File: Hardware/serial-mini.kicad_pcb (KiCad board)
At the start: 4 copper layers, 97 x 42 mm, 79 parts, among them J1 PICKIT V3 Header, J2 10103593-0001LF, J3 Serial Port, Q1 IRLML2060, Q2 IRLML2060, Q3 IRLML2060, U1 MAX232, U2 SN74AHC14RGYR, U3 DSPIC33CK64MP102, U4 MIC5504-3.3YM5-TR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

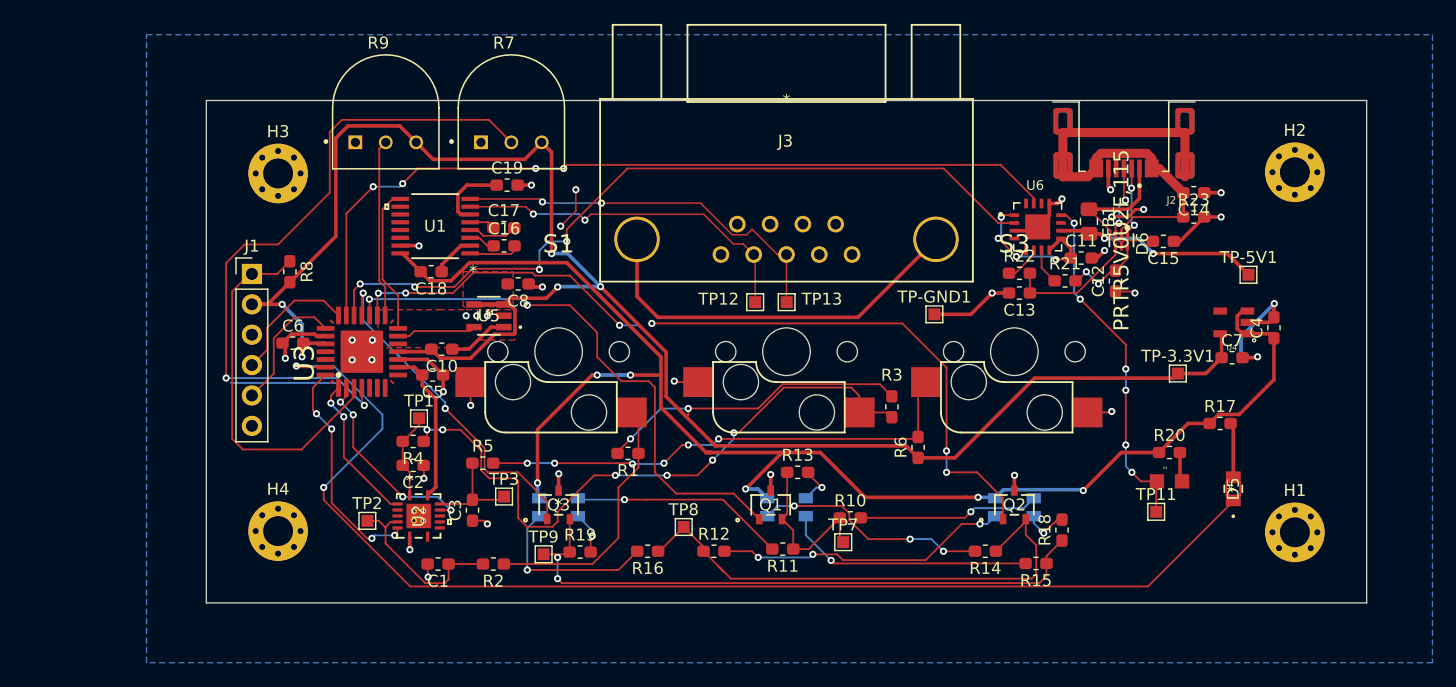
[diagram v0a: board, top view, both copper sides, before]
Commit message: Fix incorrect footprints
Fixed incorrect footprint for IRLML2060 and updated LED values to use CLVBA-FKA.
Also started deleting unneccessary test points
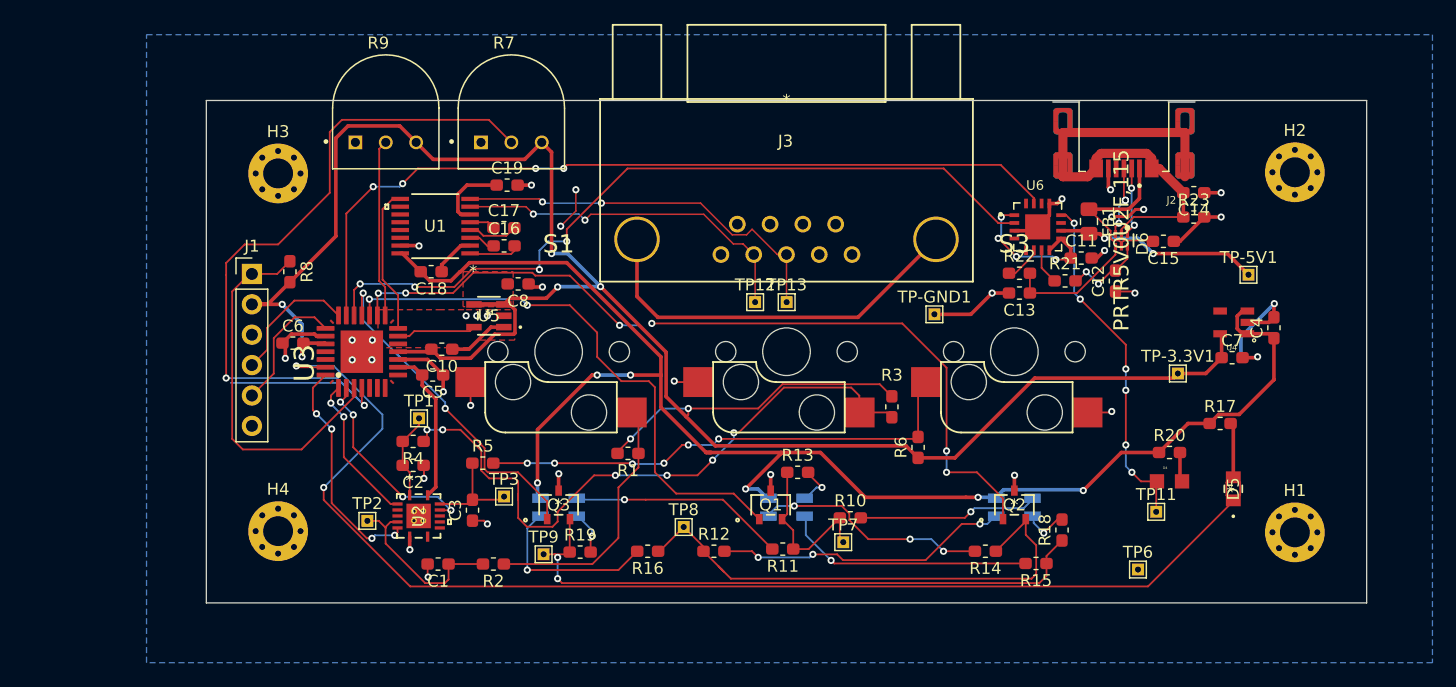
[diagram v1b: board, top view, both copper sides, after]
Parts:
- added TP6: TestPoint, TestPoint:TestPoint_THTPad_1.0x1.0mm_Drill0.5mm, F.Cu at (164.1, 108.5)
- D1, D2, D3: footprint footprints:CLVBA-FKA-CAEDH8BBB7A363 -> footprints:SOL150P350X210-4N
- R10, R11, R13: value 74 -> 100
- R12, R14, R16: value 130 -> 155
- R15, R18, R19: value 90 -> 100
- TP-3.3V1, TP-5V1, TP-GND1, TP1, TP11, TP12, TP13, TP2, TP3, TP7, TP8, TP9: footprint TestPoint:TestPoint_Pad_1.0x1.0mm -> TestPoint:TestPoint_THTPad_1.0x1.0mm_Drill0.5mm
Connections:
- Q1 pad 2: /Backlight/1.7V@69mA -> GND
- Q1 pad 3: GND -> /Backlight/2V@60mA
- Q2 pad 2: /Backlight/3V@69mA -> GND
- Q2 pad 3: GND -> /Backlight/3.1V@60mA
- Q3 pad 2: /Backlight/1.7V@57mA -> GND
- Q3 pad 3: GND -> /Backlight/2V@60mA
- R10 pad 1: /Backlight/1.7V@69mA -> /Backlight/2V@60mA
- R11 pad 1: /Backlight/1.7V@69mA -> /Backlight/2V@60mA
- R12 pad 1: /Backlight/3V@69mA -> /Backlight/3.1V@60mA
- R13 pad 1: /Backlight/1.7V@69mA -> /Backlight/2V@60mA
- R14 pad 1: /Backlight/3V@69mA -> /Backlight/3.1V@60mA
- R15 pad 1: /Backlight/1.7V@57mA -> /Backlight/2V@60mA
- R16 pad 1: /Backlight/3V@69mA -> /Backlight/3.1V@60mA
- R18 pad 1: /Backlight/1.7V@57mA -> /Backlight/2V@60mA
- R19 pad 1: /Backlight/1.7V@57mA -> /Backlight/2V@60mA
- TP7 pad 1: /Backlight/1.7V@69mA -> /Backlight/2V@60mA
- TP8 pad 1: /Backlight/3V@69mA -> /Backlight/3.1V@60mA
- TP9 pad 1: /Backlight/1.7V@57mA -> /Backlight/2V@60mA
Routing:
- net GND: track 75.9 -> 71.8 mm, vias 35 -> 32
- net /Backlight/2V@60mA: track 0.00 -> 2.76 mm, vias 0 -> 2
- net /Backlight/3.1V@60mA: track 0.00 -> 1.29 mm, vias 0 -> 1

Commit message: Fix DRC errors
Courtyard overlaps
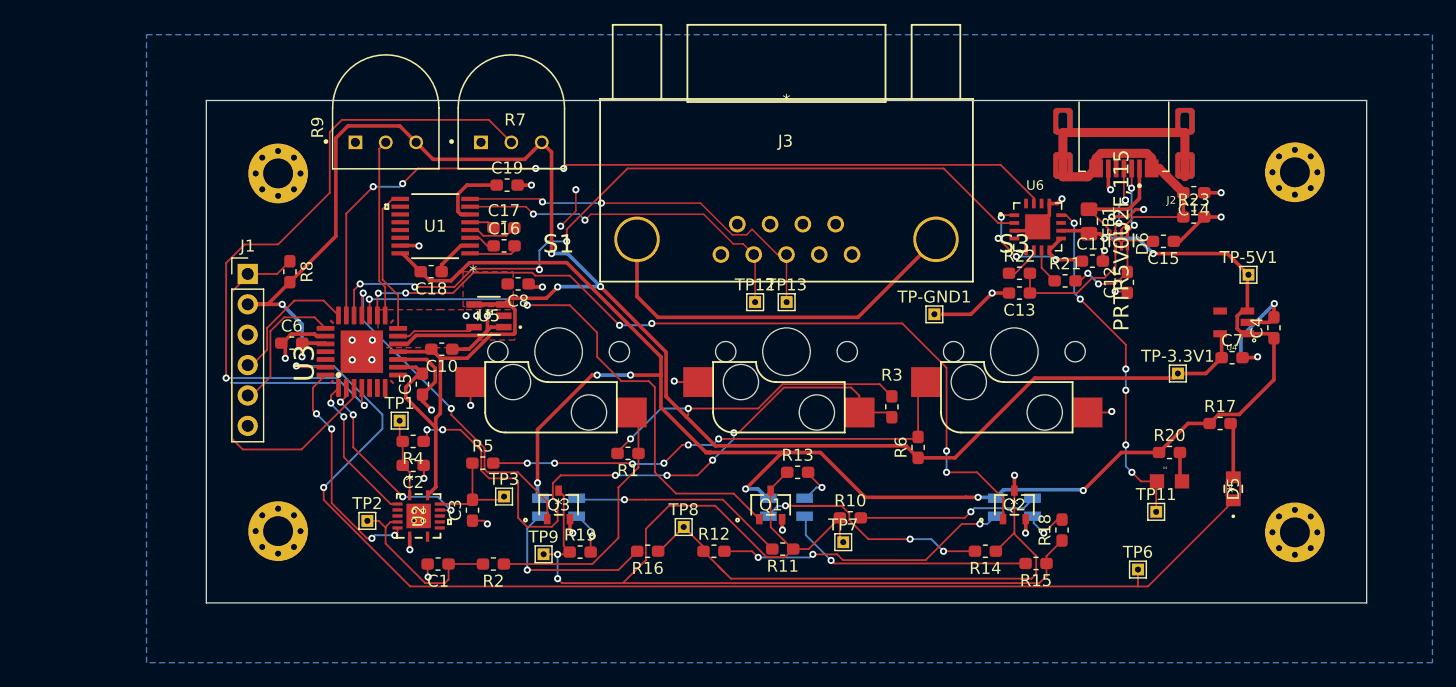
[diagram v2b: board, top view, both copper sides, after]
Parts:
- moved TP1 1.63 mm to (102.4, 96.0)
- moved C5 1.15 mm to (104.3, 93.0), turned to 90 degrees
- moved C12 1.00 mm to (163.2, 84.5)
- moved C11 0.97 mm to (160.3, 82.7)
- moved J1 0.35 mm to (89.7, 83.7)
- moved C6 0.10 mm to (93.3, 89.5)
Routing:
- net /Backlight/2V@60mA: track 2.76 -> 90.1 mm
- net /Backlight/1.7V@57mA: track 51.9 -> 0.00 mm, vias 2 -> 0
- net /Backlight/3.1V@60mA: track 1.29 -> 46.7 mm
- net /Backlight/3V@69mA: track 44.2 -> 0.00 mm
- net /Backlight/1.7V@69mA: track 14.1 -> 0.00 mm
- net GND: track 71.8 -> 85.4 mm, vias 32 -> 35
- net +3V3: track 194.4 -> 201.9 mm
- net Net-(D2-Pad1): track 19.6 -> 23.6 mm
- net +5V: track 140.4 -> 143.4 mm
- net Net-(C12-Pad2): track 7.99 -> 10.1 mm
- net Net-(R3-Pad2): track 54.3 -> 56.3 mm
- net Net-(C13-Pad1): track 11.0 -> 12.5 mm
- net /Status: track 102.5 -> 103.9 mm
- net /Red: track 68.4 -> 69.6 mm
- net Net-(C2-Pad2): track 7.59 -> 6.93 mm
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
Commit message: Adjust all track/text widths
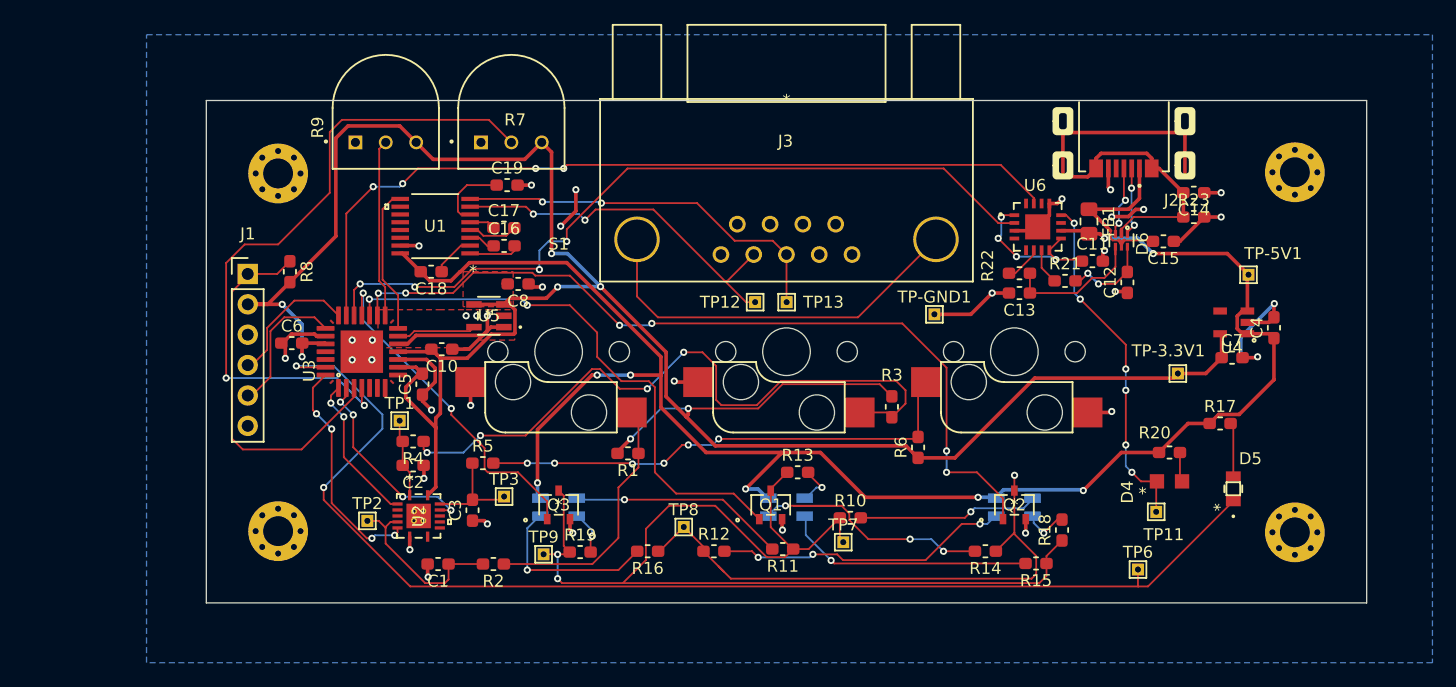
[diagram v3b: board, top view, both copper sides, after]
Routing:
- net /Brightness: track 68.2 -> 58.9 mm
- net /TTL to RS232 Converter/RS232-RX: track 29.8 -> 31.4 mm
- net Net-(R3-Pad2): track 56.3 -> 56.9 mm, vias 6 -> 4
- net /USB to UART/D+: vias 3 -> 2
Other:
- net class Default: clearance 0.127 -> 0.0762; trace_width 0.127 -> 0.1524
- net class Power added: clearance 0.0762, trace_width 0.3048, via_dia 0.6, via_drill 0.3
- rule trace_clearance: 0.127 -> 0.0762
- rule trace_min: 0.127 -> 0.1524

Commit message: Finish placing footprint labels
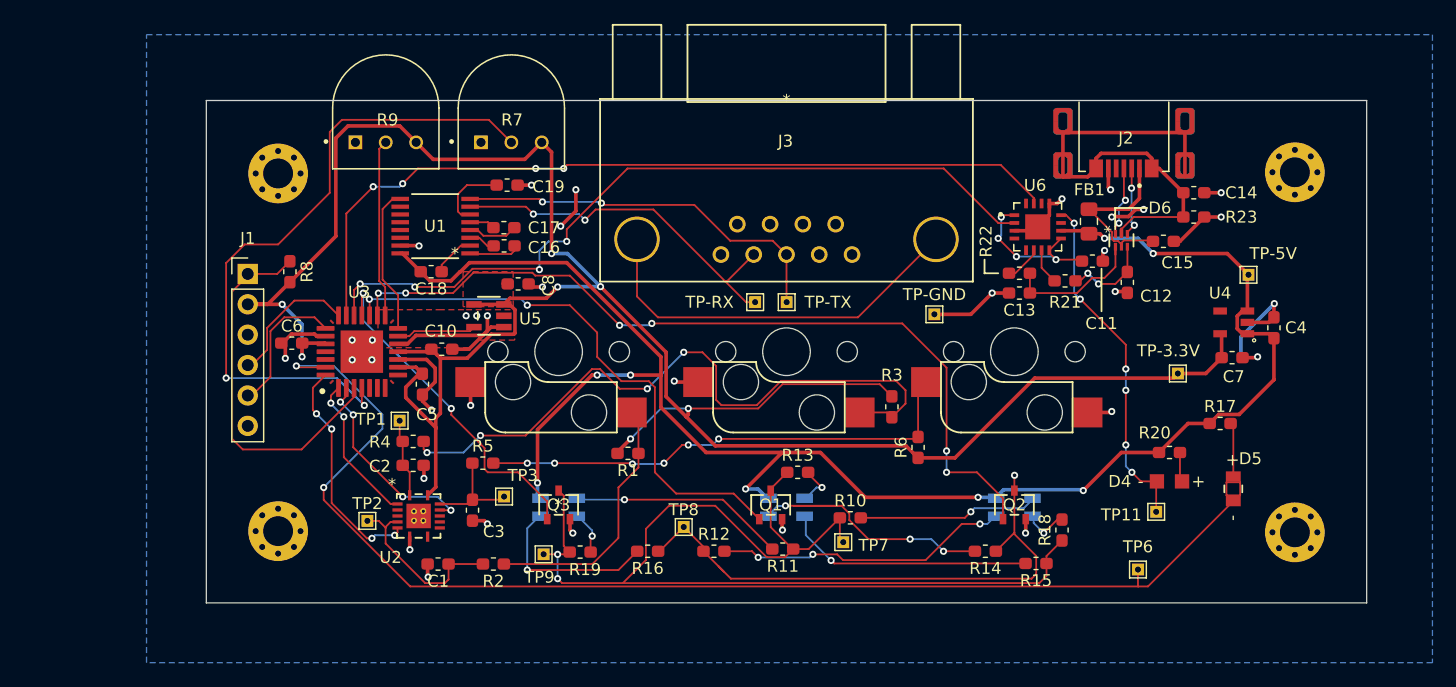
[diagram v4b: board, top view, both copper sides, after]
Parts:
- D5: value VAOL-S8WR4 -> LED_VCCLITE_0805_VCC
- U2: value SN74AHC14RGYR -> RGY14_2P05X2P05
- U5: value SIT2001BI-S2-33S-100.000000D -> SOT_SiT1630-S
- renumbered TP-3.3V1 to TP-3.3V, TP-5V1 to TP-5V, TP-GND1 to TP-GND, TP12 to TP-RX, TP13 to TP-TX

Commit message: Fix faulty debounce circuit
Used wrong value resistor/misplaced on each switch.
Also adjusted value of RC circuits for a time constant of 1 microsecond (was 1 millisecond before)
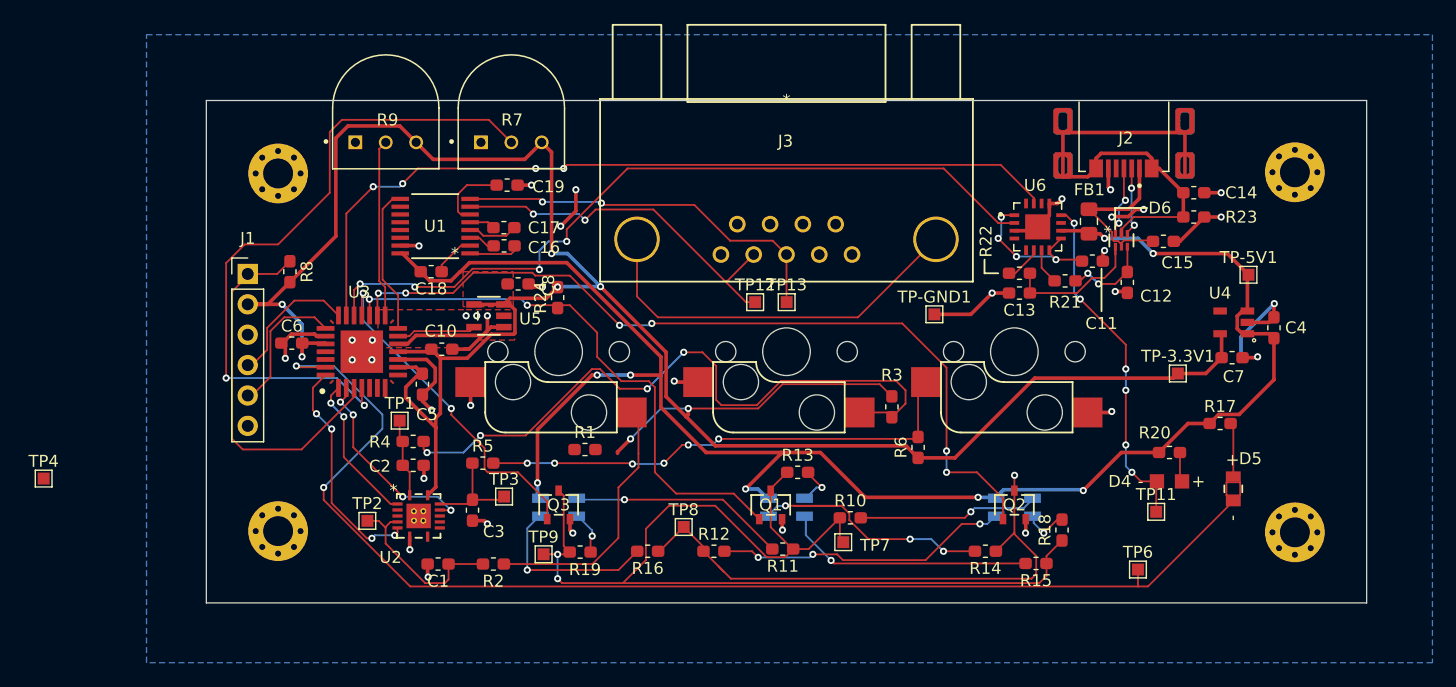
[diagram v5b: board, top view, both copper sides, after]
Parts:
- added R24: 10k, Resistor_SMD:R_0603_1608Metric_Pad1.05x0.95mm_HandSolder, F.Cu at (115.6, 85.7)
- added TP4: TestPoint, TestPoint:TestPoint_Pad_1.0x1.0mm, F.Cu at (72.6, 100.9)
- C1, C2, C3: value 0.1UF -> 10nF
- D5: value LED_VCCLITE_0805_VCC -> VAOL-S8WR4
- R17: value 133 -> 100
- R2, R4, R5: value 10k -> 1k
- TP-3.3V1: renamed from TP-3.3V; footprint TestPoint:TestPoint_THTPad_1.0x1.0mm_Drill0.5mm -> TestPoint:TestPoint_Pad_1.0x1.0mm
- TP-5V1: renamed from TP-5V; footprint TestPoint:TestPoint_THTPad_1.0x1.0mm_Drill0.5mm -> TestPoint:TestPoint_Pad_1.0x1.0mm
- TP-GND1: renamed from TP-GND; footprint TestPoint:TestPoint_THTPad_1.0x1.0mm_Drill0.5mm -> TestPoint:TestPoint_Pad_1.0x1.0mm
- TP1, TP11, TP2, TP3, TP6, TP7, TP8, TP9: footprint TestPoint:TestPoint_THTPad_1.0x1.0mm_Drill0.5mm -> TestPoint:TestPoint_Pad_1.0x1.0mm
- TP12: renamed from TP-RX; footprint TestPoint:TestPoint_THTPad_1.0x1.0mm_Drill0.5mm -> TestPoint:TestPoint_Pad_1.0x1.0mm
- TP13: renamed from TP-TX; footprint TestPoint:TestPoint_THTPad_1.0x1.0mm_Drill0.5mm -> TestPoint:TestPoint_Pad_1.0x1.0mm
- U2: value RGY14_2P05X2P05 -> SN74AHC14RGYR
- U5: value SOT_SiT1630-S -> SIT2001BI-S2-33S-100.000000D
- moved R1 3.61 mm to (117.9, 98.4), turned to 0 degrees
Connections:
- R1 pad 1: Net-(R1-Pad1) -> Net-(C1-Pad1)
- R2 pad 1: Net-(R1-Pad1) -> Net-(R2-Pad1)
- R3 pad 2: Net-(R3-Pad2) -> Net-(C2-Pad2)
- R4 pad 1: Net-(R3-Pad2) -> Net-(R4-Pad1)
- R6 pad 2: Net-(R5-Pad2) -> Net-(C3-Pad2)
- S1 pad 2: Net-(R1-Pad1) -> Net-(R2-Pad1)
- S2 pad 2: Net-(R3-Pad2) -> Net-(R4-Pad1)
- U5 pad 3: +3V3 -> Net-(R24-Pad1)
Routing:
- net Net-(R2-Pad1): track 0.00 -> 21.9 mm
- net Net-(R1-Pad1): track 21.9 -> 0.00 mm

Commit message: Fix weird routing
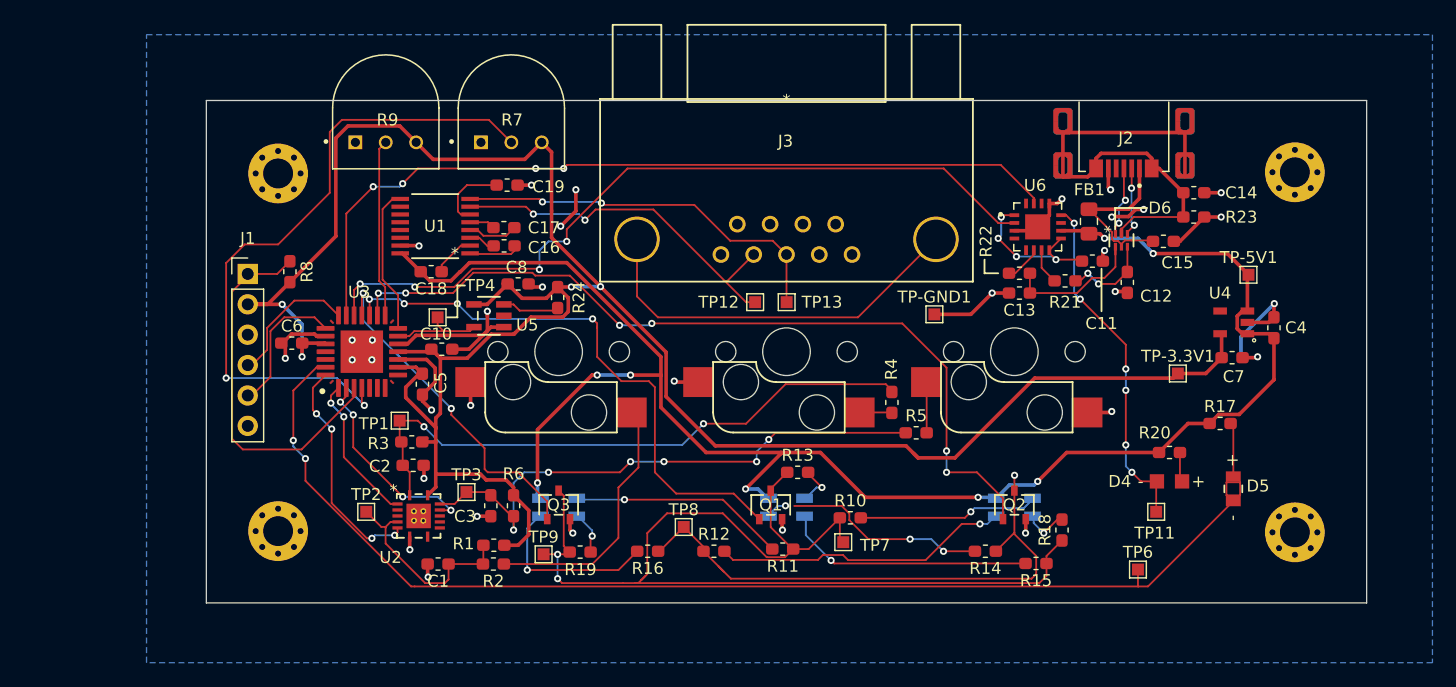
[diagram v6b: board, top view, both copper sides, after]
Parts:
- moved R3 40.2 mm to (103.4, 97.8), turned to 180 degrees
- moved R4 40.2 mm to (143.5, 94.5), turned to 90 degrees
- moved R5 36.3 mm to (145.5, 97.0)
- moved TP4 35.6 mm to (105.5, 87.4)
- moved R6 34.2 mm to (111.9, 103.1), turned to 270 degrees
- moved R1 11.0 mm to (110.2, 106.4)
- moved TP3 3.17 mm to (108.0, 102.0)
- moved C3 1.58 mm to (110.0, 103.1)
- moved TP2 0.76 mm to (99.6, 103.6)
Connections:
- TP4 pad 1: Net-(TP4-Pad1) -> /OSCO
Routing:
- net Net-(R3-Pad2): track 56.9 -> 0.00 mm, vias 4 -> 0
- net Net-(C2-Pad2): track 6.93 -> 51.4 mm, vias 0 -> 2
- net Net-(C3-Pad2): track 8.69 -> 47.5 mm, vias 0 -> 6
- net Net-(R5-Pad2): track 41.4 -> 5.23 mm, vias 6 -> 0
- net /Status: track 103.9 -> 97.1 mm
- net +3V3: track 201.9 -> 195.9 mm, vias 7 -> 4
- net Net-(R24-Pad1): track 0.00 -> 5.28 mm
- net Net-(D2-Pad1): track 23.6 -> 18.9 mm
- net Net-(R4-Pad1): track 0.00 -> 2.47 mm
- net Net-(C1-Pad1): track 15.2 -> 17.2 mm
- net /OSCO: track 6.65 -> 8.15 mm
- net /Backlight/2V@60mA: track 90.1 -> 89.5 mm
- net /Green: track 46.9 -> 47.5 mm, vias 2 -> 4
- net GND: track 85.4 -> 85.6 mm, vias 35 -> 33
- net Net-(D1-Pad1): track 24.7 -> 24.8 mm, vias 3 -> 1
- removed copper zone on F.Cu, net +3V3
- removed copper zone on F.Cu, net GND
